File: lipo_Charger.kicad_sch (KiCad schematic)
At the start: 57 parts, among them Q1 PMOS, Q2 NMOS, Q3 NMOS, Q4 NMOS, Q5 NMOS, U1 BQ25703ARSNR

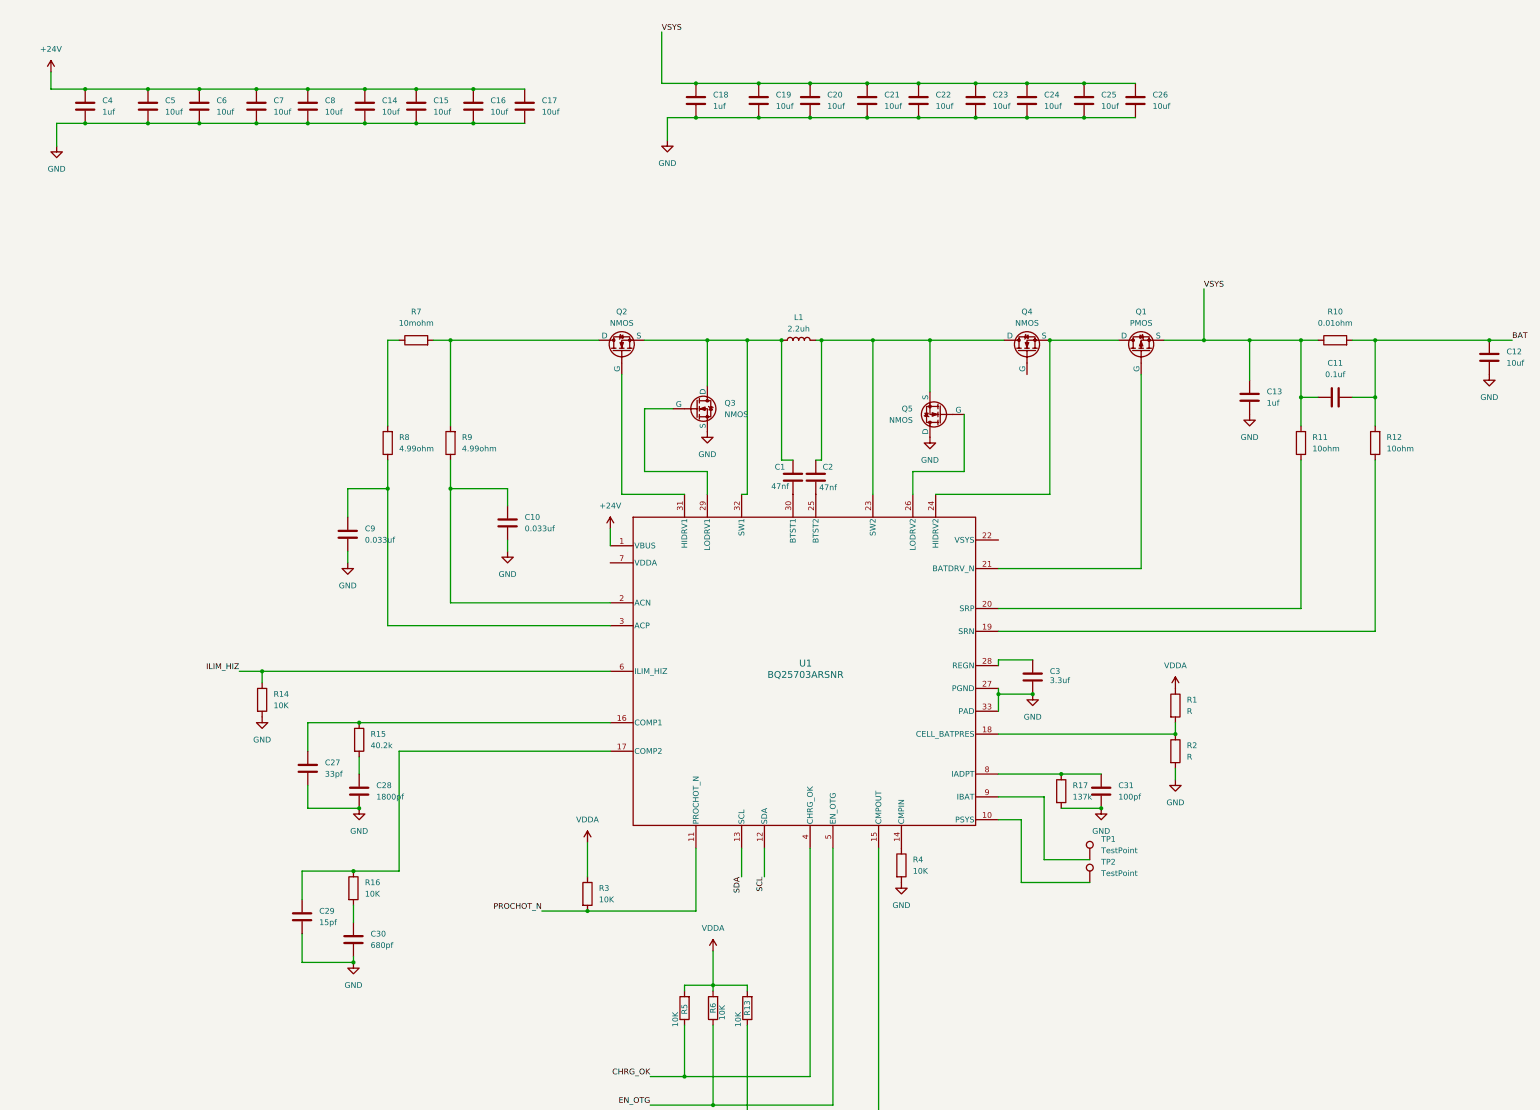
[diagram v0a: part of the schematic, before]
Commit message: three r one c balancing circuit dev board has to be done yet
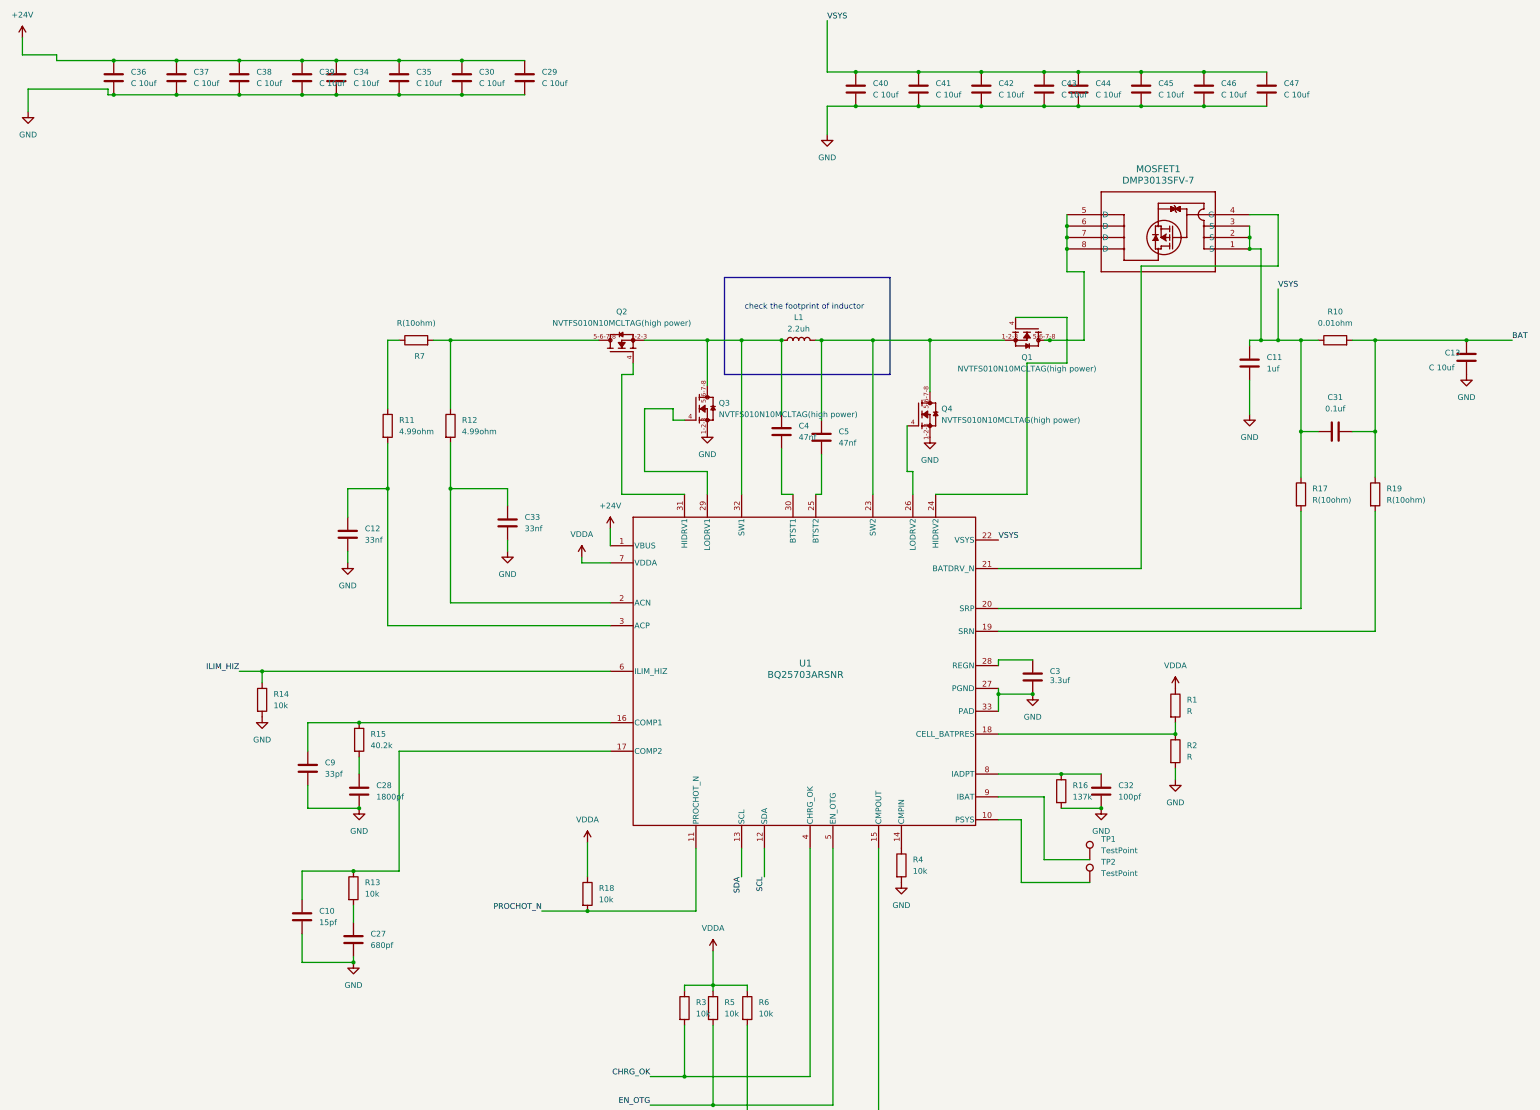
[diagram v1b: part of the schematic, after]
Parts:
- removed C1, C2: 47nf, symbol Device:C
- removed C10, C9: 0.033uf, symbol Device:C
- removed C11: 0.1uf, symbol Device:C
- removed C12, C14, C15, C16, C17, C19, C20, C21, C22, C23, C24, C25, C26, C5, C6, C7, C8: 10uf, symbol Device:C
- removed C13, C18, C4: 1uf, symbol Device:C
- removed C27: 33pf, symbol Device:C
- removed C29: 15pf, symbol Device:C
- removed C30: 680pf, symbol Device:C
- removed C31: 100pf, symbol Device:C
- removed Q1: PMOS, symbol Simulation_SPICE:PMOS
- removed Q2, Q3, Q4, Q5: NMOS, symbol Simulation_SPICE:NMOS
- removed R11, R12: 10ohm, symbol Device:R
- removed R13, R14, R16, R3, R4, R5, R6: 10K, symbol Device:R
- removed R15: 40.2k, symbol Device:R
- removed R17: 137k, symbol Device:R
- removed R7: 10mohm, symbol Device:R
- removed R8, R9: 4.99ohm, symbol Device:R
- added C10: 15pf, Capacitor_SMD:C_0402_1005Metric_Pad0.74x0.62mm_HandSolder, symbol Lipo_charger_sym:15pf
- added C11: 1uf, Capacitor_SMD:C_0805_2012Metric_Pad1.18x1.45mm_HandSolder, symbol Lipo_charger_sym:1uf
- added C12, C33: 33nf, Capacitor_SMD:C_0805_2012Metric_Pad1.18x1.45mm_HandSolder, symbol Lipo_charger_sym:33nf
- added C13, C29, C30, C34, C35, C36, C37, C38, C39, C40, C41, C42, C43, C44, C45, C46, C47: C 10uf, Capacitor_SMD:C_0805_2012Metric_Pad1.18x1.45mm_HandSolder, symbol Lipo_charger_sym:C 10uf
- added C27: 680pf, Capacitor_SMD:C_0603_1608Metric_Pad1.08x0.95mm_HandSolder, symbol Lipo_charger_sym:680pf
- added C31: 0.1uf, Capacitor_SMD:C_0603_1608Metric_Pad1.08x0.95mm_HandSolder, symbol Lipo_charger_sym:0.1uf
- added C32: 100pf, Capacitor_SMD:C_0603_1608Metric_Pad1.08x0.95mm_HandSolder, symbol Lipo_charger_sym:100pf
- added C4, C5: 47nf, Capacitor_SMD:C_0603_1608Metric_Pad1.08x0.95mm_HandSolder, symbol Lipo_charger_sym:47nf
- added C9: 33pf, Capacitor_SMD:C_0805_2012Metric_Pad1.18x1.45mm_HandSolder, symbol Lipo_charger_sym:33pf
- added MOSFET1: DMP3013SFV-7, Lipo_Charger_footprint:POWERDI3333-8_UX_DIO-M, symbol Lipo_charger_sym:DMP3013SFV-7
- added Q1, Q2, Q3, Q4: NVTFS010N10MCLTAG(high power), Lipo_Charger_footprint:TRANS_NVTFS010N10MCLTAG(nch high power), symbol Lipo_charger_sym:NVTFS010N10MCLTAG(high power)
- added R11, R12: 4.99ohm, Inductor_SMD:L_0805_2012Metric_Pad1.05x1.20mm_HandSolder, symbol Lipo_charger_sym:4.99ohm
- added R13, R14, R18, R3, R4, R5, R6: 10k, Inductor_SMD:L_0805_2012Metric_Pad1.05x1.20mm_HandSolder, symbol Lipo_charger_sym:R(10k)
- added R15: 40.2k, Resistor_SMD:R_0603_1608Metric_Pad0.98x0.95mm_HandSolder, symbol Lipo_charger_sym:40.2k
- added R16: 137k, Resistor_SMD:R_0402_1005Metric_Pad0.72x0.64mm_HandSolder, symbol Lipo_charger_sym:137k
- added R17, R19, R7: R(10ohm), Resistor_SMD:R_0603_1608Metric_Pad0.98x0.95mm_HandSolder, symbol Lipo_charger_sym:R(10ohm)
- L1: footprint (none) -> Inductor_SMD:L_10.4x10.4_H4.8
- TP1, TP2: footprint (none) -> TestPoint:TestPoint_Pad_2.0x2.0mm
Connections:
- net +24V: now also C29.1, C30.1, C34.1, C35.1, C36.1, C37.1, C38.1, C39.1
- net BAT: now also C13.1, C31.2, R19.1
- net CHRG_OK: now also R3.2
- net CMPOUT: now also R6.2
- net EN_OTG: now also R5.2
- net GND: now also C10.2, C11.2, C12.2, C13.2, C27.2, C29.2, C30.2, C32.2, C33.2, C34.2, C35.2, C36.2, C37.2, C38.2, C39.2, C40.2, C41.2, C42.2, C43.2, C44.2, C45.2, C46.2, C47.2, C9.2, Q3.1-2-3, Q4.1-2-3, R14.2, R16.2, R4.2
- net ILIM_HIZ: now also R14.1
- net PROCHOT_N: now also R18.2
- net VDDA: now also U1.7 (VDDA), R18.1, R3.1, R5.1, R6.1
- net VSYS: now also U1.22 (VSYS), C11.1, C31.1, C40.1, C41.1, C42.1, C43.1, C44.1, C45.1, C46.1, C47.1, MOSFET1.1 (S), MOSFET1.2 (S), MOSFET1.3 (S), R17.1
- net at C28.1: now also R15.2
- net at L1.2, U1.23 (SW2): now also C5.1, Q1.1-2-3, Q4.5-6-7-8
- net at U1.24 (HIDRV2): now also Q1.4
- net at U1.26 (LODRV2): now also Q4.4
- net at U1.8 (IADPT): now also C32.1, R16.1
- net at U1.14 (CMPIN): now also R4.1
- net at U1.16 (COMP1): now also C9.1, R15.1
- net at U1.17 (COMP2): now also C10.1, R13.1
- net at U1.19 (SRN): now also R19.2
- net at U1.2 (ACN): now also C33.1, R12.2
- net at U1.20 (SRP): now also R17.2
- net at U1.21 (BATDRV_N): now also MOSFET1.4 (G)
- net at U1.25 (BTST2): now also C5.2
- net at U1.29 (LODRV1): now also Q3.4
- net at U1.3 (ACP): now also C12.1, R11.2
- net at U1.30 (BTST1): now also C4.2
- net at U1.31 (HIDRV1): now also Q2.4
- net at L1.1, U1.32 (SW1): now also C4.1, Q2.1-2-3, Q3.5-6-7-8
- new net: MOSFET1.5 (D), MOSFET1.6 (D), MOSFET1.7 (D), MOSFET1.8 (D), Q1.5-6-7-8
- new net: R11.1, R7.1
- new net: Q2.5-6-7-8, R12.1, R7.2
- new net: C27.1, R13.2
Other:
- note added: "check the footprint of inductor"

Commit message: adcc has to be done stm dev board if needed has to be inccluded
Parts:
- removed R1, R2: R, symbol Device:R
- added J1: XT60-M, Connector_AMASS:AMASS_XT60-M_1x02_P7.20mm_Vertical, symbol mazebot:XT60-M
- added J2: Conn_01x05, Connector_JST:JST_XH_B5B-XH-A_1x05_P2.50mm_Vertical, symbol Connector_Generic:Conn_01x05
- added J3: Conn_01x04, Connector_PinHeader_2.54mm:PinHeader_1x04_P2.54mm_Vertical, symbol Connector_Generic:Conn_01x04
- added MOSFET2, MOSFET3, MOSFET4, MOSFET5: DMP3013SFV-7, Lipo_Charger_footprint:POWERDI3333-8_UX_DIO-M, symbol Lipo_charger_sym:DMP3013SFV-7
- added Q5, Q6, Q7, Q8: NX7002AK_215(nch low power), Lipo_Charger_footprint:SOT95P230X110-3N(nch low power), symbol Lipo_charger_sym:NX7002AK_215(nch low power)
- added R1, R20, R21, R22, R23, R24, R25, R30, R31, R8, R9: 10k, Inductor_SMD:L_0805_2012Metric_Pad1.05x1.20mm_HandSolder, symbol Lipo_charger_sym:R(10k)
- added R2: 40.2k, Resistor_SMD:R_0603_1608Metric_Pad0.98x0.95mm_HandSolder, symbol Lipo_charger_sym:40.2k
- added R26, R27, R28, R29: R, Resistor_SMD:R_2512_6332Metric_Pad1.40x3.35mm_HandSolder, symbol Device:R
- C28: footprint (none) -> Capacitor_SMD:C_0805_2012Metric_Pad1.18x1.45mm_HandSolder
- C3: value 3.3uf -> 2.2uf; footprint (none) -> Diode_SMD:D_1206_3216Metric_Pad1.42x1.75mm_HandSolder
- R10: footprint (none) -> Resistor_SMD:R_2512_6332Metric_Pad1.40x3.35mm_HandSolder
- U1: link https://robu.in/product/cdrh104r-2-2%ce%bch-power-inductor-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 -> https://robu.in/product/bq25713rsnr-texas-instruments-3-5v2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
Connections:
- net +24V: now also R11.1, R7.1
- net BAT: now also J1.P (POS)
- net GND: now also J1.N (NEG), J2.5 (Pin_5), J3.1 (Pin_1), Q5.2, Q6.2, Q7.2, Q8.2, R2.2, R20.2, R22.2, R24.2, R28.2, R9.2
- net SCL: now also J3.3 (Pin_3), R30.2
- net SDA: now also J3.4 (Pin_4), R31.2
- net VDDA: now also J3.2 (Pin_2), R1.1, R30.1, R31.1
- net at U1.18 (CELL_BATPRES): now also R1.2, R2.1
- new net: Q7.1, R22.1
- new net: Q8.1, R24.1
- new net: MOSFET5.4 (G), Q8.3, R25.2
- new net: MOSFET4.4 (G), Q7.3, R23.2
- new net: MOSFET4.5 (D), MOSFET4.6 (D), MOSFET4.7 (D), MOSFET4.8 (D), R26.1
- new net: MOSFET2.5 (D), MOSFET2.6 (D), MOSFET2.7 (D), MOSFET2.8 (D), R29.1
- new net: Q5.1, R9.1
- new net: MOSFET3.5 (D), MOSFET3.6 (D), MOSFET3.7 (D), MOSFET3.8 (D), R27.1
- new net: MOSFET2.4 (G), Q5.3, R8.2
- new net: MOSFET3.2 (S), MOSFET3.3 (S), R21.1
- new net: MOSFET3.4 (G), Q6.3, R21.2
- new net: Q6.1, R20.1
- new net: MOSFET5.5 (D), MOSFET5.6 (D), MOSFET5.7 (D), MOSFET5.8 (D), R28.1
- new net CELLL_2S: J2.3 (Pin_3), MOSFET4.1 (S), MOSFET4.2 (S), MOSFET4.3 (S), R23.1, R27.2
- new net CELL_1S: J2.4 (Pin_4), MOSFET5.1 (S), MOSFET5.2 (S), MOSFET5.3 (S), R25.1, R26.2
- new net CELL_3S: J2.2 (Pin_2), MOSFET3.1 (S), R29.2
- new net CELL_4S: J2.1 (Pin_1), MOSFET2.1 (S), MOSFET2.2 (S), MOSFET2.3 (S), R8.1
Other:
- moved on the sheet: Q1, R3, R5, R6

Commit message: need to checked sch and then routing thickness has to be calculated and ground fill has to be added
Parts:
- removed J1: XT60-M, Connector_AMASS:AMASS_XT60-M_1x02_P7.20mm_Vertical, symbol mazebot:XT60-M
- removed R26, R27, R28, R29: R, Resistor_SMD:R_2512_6332Metric_Pad1.40x3.35mm_HandSolder, symbol Device:R
- added C30, C31, C32, C33, C34: 1uf, Capacitor_SMD:C_0805_2012Metric_Pad1.18x1.45mm_HandSolder, symbol Lipo_charger_sym:1uf
- added J1: Conn_01x02_Pin, Connector_AMASS:AMASS_XT60-M_1x02_P7.20mm_Vertical, symbol Connector:Conn_01x02_Pin
- added J4: Conn_01x05, Connector_PinHeader_2.54mm:PinHeader_1x05_P2.54mm_Vertical, symbol Connector_Generic:Conn_01x05
- added J5: Conn_01x04, Connector_PinHeader_2.54mm:PinHeader_1x04_P2.54mm_Vertical, symbol Connector_Generic:Conn_01x04
- added R14, R2, R22, R5: R, Resistor_SMD:R_2512_6332Metric_Pad1.40x3.35mm_HandSolder, symbol Device:R
- added R32: 27k, Resistor_SMD:R_0603_1608Metric_Pad0.98x0.95mm_HandSolder, symbol Lipo_charger_sym:27k
- added R33: 15k, Resistor_SMD:R_0603_1608Metric_Pad0.98x0.95mm_HandSolder, symbol Lipo_charger_sym:15k
- added R34: 3.3k, Resistor_SMD:R_0603_1608Metric_Pad0.98x0.95mm_HandSolder, symbol Lipo_charger_sym:3.3k
- added R35, R36: 39k, Resistor_SMD:R_0603_1608Metric_Pad0.98x0.95mm_HandSolder, symbol Lipo_charger_sym:39k
- added R37, R38, R39, R40, R41: 8.2k, Resistor_SMD:R_0603_1608Metric_Pad0.98x0.95mm_HandSolder, symbol Lipo_charger_sym:8.2k
- added TP3: TestPoint, TestPoint:TestPoint_Pad_4.0x4.0mm, symbol Connector:TestPoint
- R10: value 0.01ohm -> R
- renumbered C36 to C1, C41 to C10, C42 to C11, C43 to C12, C44 to C13, C45 to C14, C46 to C15, C47 to C16, C13 to C17, C11 to C18, C4 to C19, C37 to C2, C31 to C20, C5 to C21, C33 to C22, C12 to C23, C3 to C24, C9 to C25, C28 to C26, C32 to C27, C10 to C28, C27 to C29, C38 to C3, C39 to C4, C34 to C5, C35 to C6, C30 to C7, C29 to C8, C40 to C9, MOSFET2 to MOSFET1, MOSFET1 to MOSFET2, Q5 to Q1, Q1 to Q3, Q3 to Q4, Q4 to Q5, R8 to R1, R17 to R11, R19 to R12, R23 to R13, R22 to R15, R25 to R16, R14 to R17, R1 to R18, R15 to R19, R2 to R20, R24 to R21, R16 to R23, R4 to R24, R13 to R25, R18 to R26, R30 to R27, R31 to R28, R3 to R29, R9 to R3, R5 to R30, R6 to R31, R7 to R4, R21 to R6, R11 to R7, R12 to R8, R20 to R9
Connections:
- net +24V: now also TP3.1
- net BAT: now also J1.1 (Pin_1), R35.1, R5.2; no longer R10.2
- net CELL_1S: now also R14.2, R34.1
- net CELL_3S: now also MOSFET3.2 (S), MOSFET3.3 (S), R6.1, R2.2, R32.1
- net CELL_4S: now also R36.1
- net GND: now also C30.1, C31.1, C32.1, C33.1, C34.1, J1.2 (Pin_2), R22.2, R37.2, R38.2, R39.2, R40.2, R41.2
- net VSYS: now also R5.1; no longer R10.1
- net at Q7.1, R15.1: now also J5.2 (Pin_2)
- net at Q8.1, R21.1: now also J5.1 (Pin_1)
- net at MOSFET4.5 (D), MOSFET4.6 (D), MOSFET4.7 (D)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: now also R14.1
- net at MOSFET1.5 (D), MOSFET1.6 (D), MOSFET1.7 (D)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: now also R2.1
- net at Q1.1, R3.1: now also J5.4 (Pin_4)
- net at MOSFET3.5 (D), MOSFET3.6 (D), MOSFET3.7 (D)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: now also R10.1
- net at Q6.1, R9.1: now also J5.3 (Pin_3)
- net at MOSFET5.5 (D), MOSFET5.6 (D), MOSFET5.7 (D)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: now also R22.1
- net CELLL_2S renamed CELL_2S
- net CELL_2S: now also R10.2, R33.1
- new net BAT_adc: C33.2, J4.5 (Pin_5), R35.2, R40.1
- new net CELL_1S_adc: C30.2, J4.1 (Pin_1), R34.2, R37.1
- new net CELL_2S_adc: C32.2, J4.2 (Pin_2), R33.2, R39.1
- new net CELL_3S_adc: C31.2, J4.3 (Pin_3), R32.2, R38.1
- new net CELL_4S_adc: C34.2, J4.4 (Pin_4), R36.2, R41.1

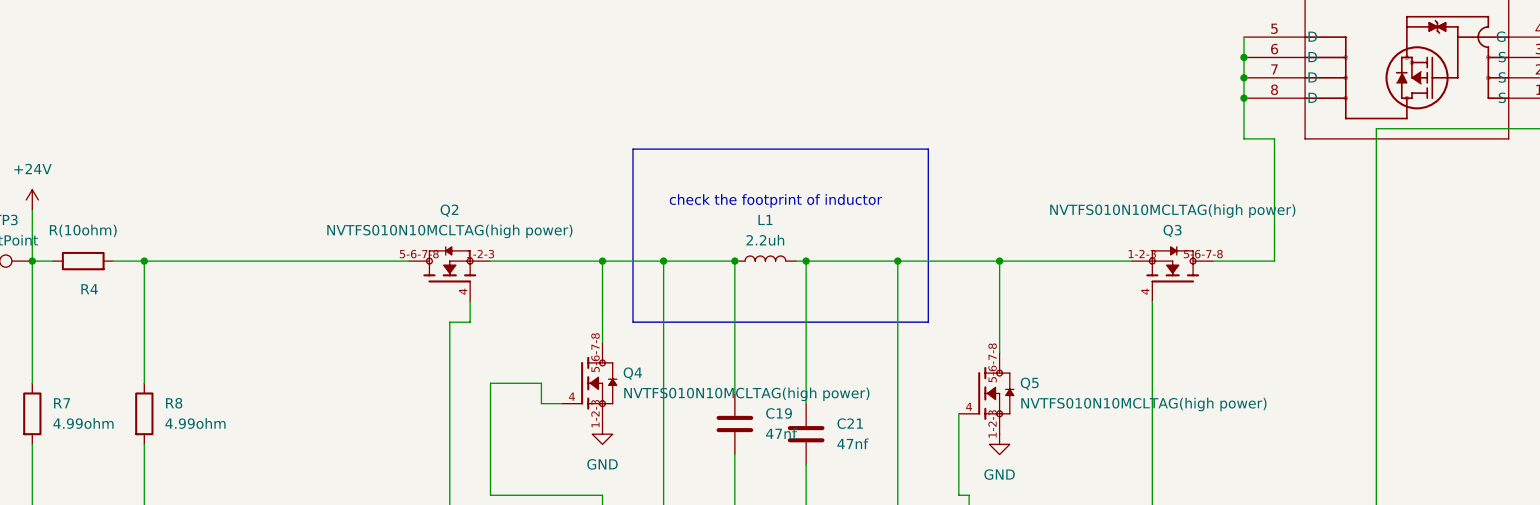
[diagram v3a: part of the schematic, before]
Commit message: need to add stm dev boarrd and silkscreen managing sch rechecik and trace width check eed to add gnd and power plane
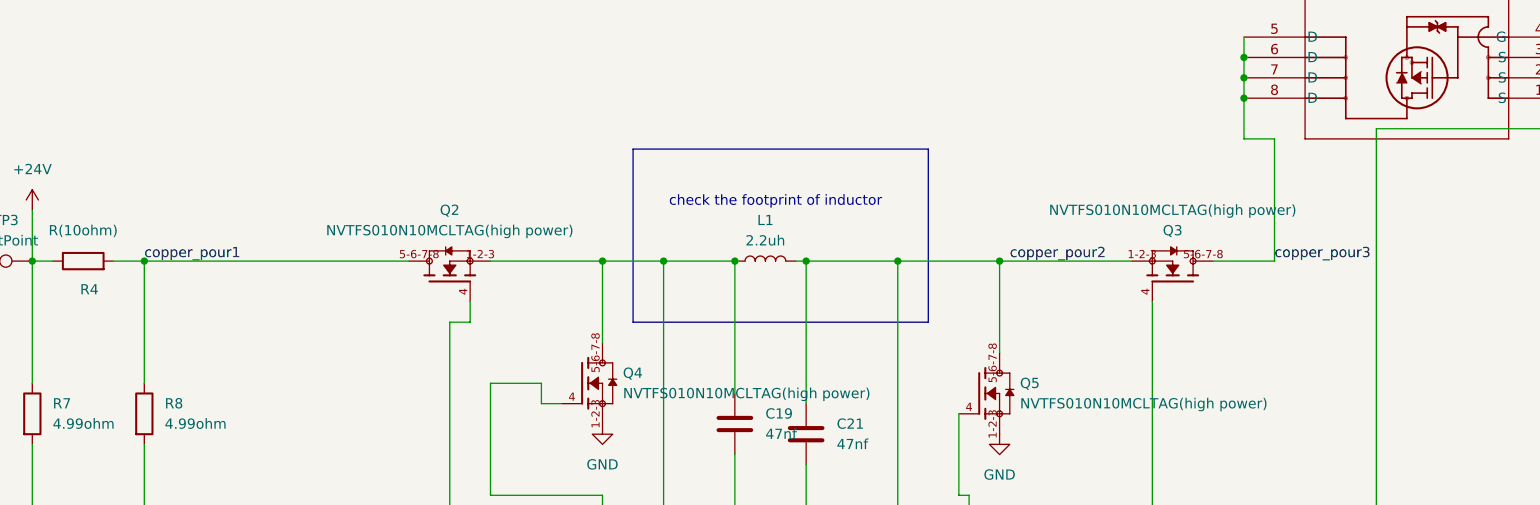
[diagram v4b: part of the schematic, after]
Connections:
- net copper_pour3: now reaches MOSFET2.5 (D), MOSFET2.6 (D), MOSFET2.7 (D), MOSFET2.8 (D), Q3.5-6-7-8
- net copper_pour1: now reaches Q2.5-6-7-8, R4.2, R8.1
- net copper_pour2: now reaches C21.1, L1.2, Q3.1-2-3, Q5.5-6-7-8, U1.23 (SW2)
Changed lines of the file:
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@@
+		)
+	)
+	(label "copper_pour3"
+		(at 251.46 90.17 0)
+		(effects
+			(font
+				(size 1.27 1.27)
+			)
+			(justify left bottom)
 		)
 	)
@@
 			)
 			(justify right bottom)
+		)
+	)
+	(label "copper_pour1"
+		(at 110.49 90.17 0)
+		(effects
+			(font
+				(size 1.27 1.27)
+			)
+			(justify left bottom)
 		)
 	)
@@
 		)
 	)
+	(label "copper_pour2"
+		(at 218.44 90.17 0)
+		(effects
+			(font
+				(size 1.27 1.27)
+			)
+			(justify left bottom)
+		)
+	)
